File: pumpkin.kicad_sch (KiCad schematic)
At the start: 26 parts, among them J1 MK-12C02

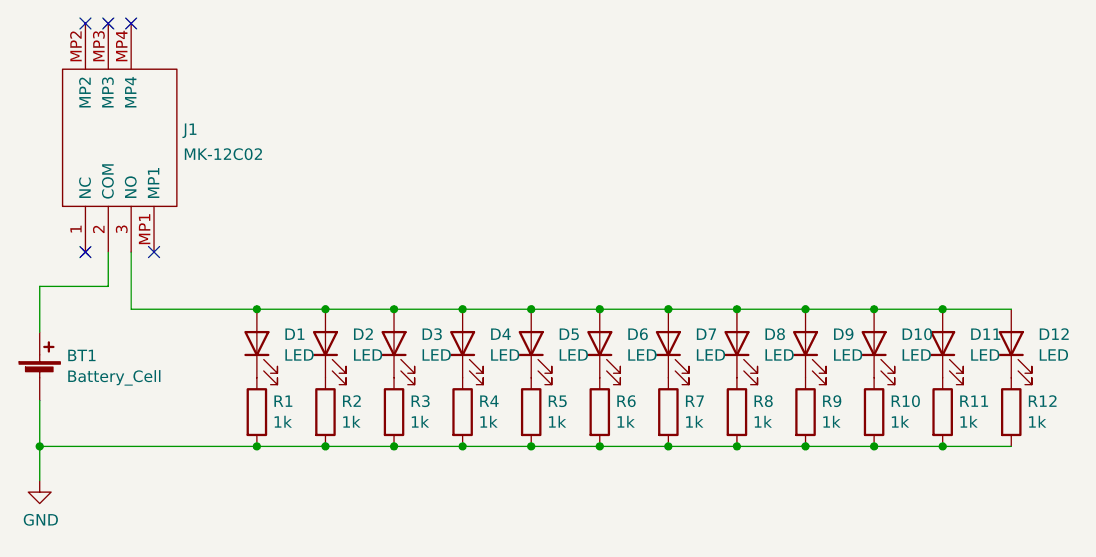
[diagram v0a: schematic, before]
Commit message: changed cr2032 to cr1225
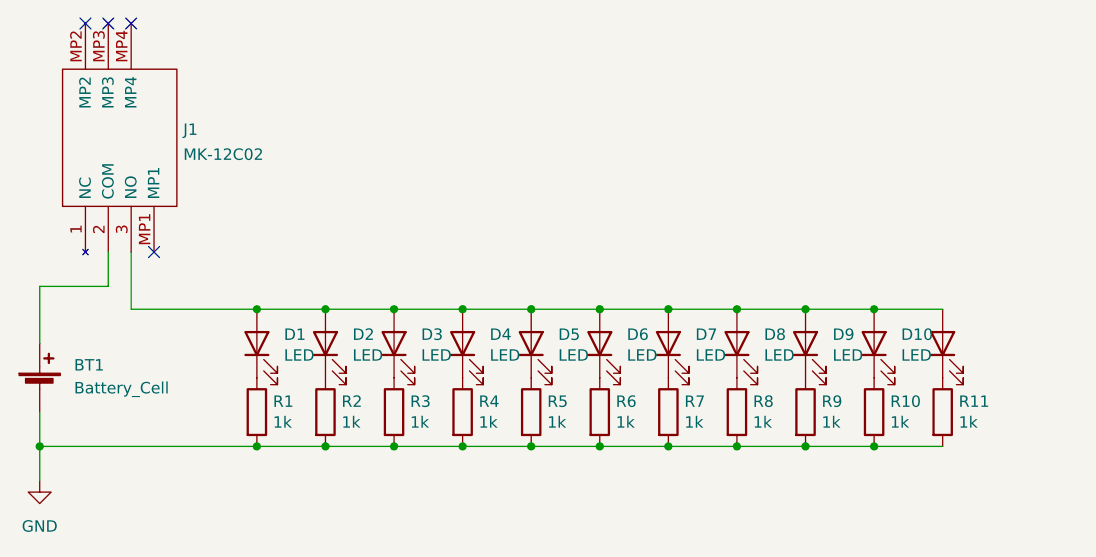
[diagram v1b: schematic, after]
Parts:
- removed D12: LED, LED_SMD:LED_0805_2012Metric_Pad1.15x1.40mm_HandSolder, symbol Device:LED
- removed R12: 1k, Resistor_SMD:R_0805_2012Metric_Pad1.20x1.40mm_HandSolder, symbol Device:R
- BT1: footprint user-footprints:CR2032_holder_ali -> Battery:BatteryHolder_LINX_BAT-HLD-012-SMT
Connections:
- no-connect marks 5 -> 4
